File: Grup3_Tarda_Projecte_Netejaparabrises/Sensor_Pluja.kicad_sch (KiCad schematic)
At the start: 0 parts

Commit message: canvis esquematic
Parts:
- added C1: 100n, symbol Device:C
- added R1, R2: R, symbol Device:R
- added RV1: 10k, symbol Device:R_Potentiometer_Trim
- added SW1: SW_SPST, symbol Switch:SW_SPST
- added U3: LM393, symbol Comparator:LM393
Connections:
- new net: R1.2, RV1.1
- new net +VCC: C1.1, R1.1, SW1.2 (B), U3.8 (V+)
- new net Comp_o: U3.1
- new net GND: C1.2, R2.2, RV1.3, U3.4 (V-)
- new net Vin+: R2.1, SW1.1 (A), U3.3 (+)
- new net Vthold: RV1.2, U3.2 (-)
- no-connect marks 0 -> 3
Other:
- note added: "DRIVER SENSOR PLUJA"
- note added: "SENSOR"
- note added: "SENSOR PLUJA"
- note added: "SUPPLY"

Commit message: canvis esquematic
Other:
- title: (none) -> Projecte Netejaparabrises - Grup 4 Tarda
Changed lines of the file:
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@@
 (kicad_sch (version 20230121) (generator eeschema)
   (paper "A4")
+  (title_block
+    (title "Projecte Netejaparabrises - Grup 4 Tarda")
+    (date "2023-03-30")
+    (rev "v1.0.30032023")
+  )
   (junction (at 181.864 102.362) (diameter 0) (color 0 0 0 0)
   )

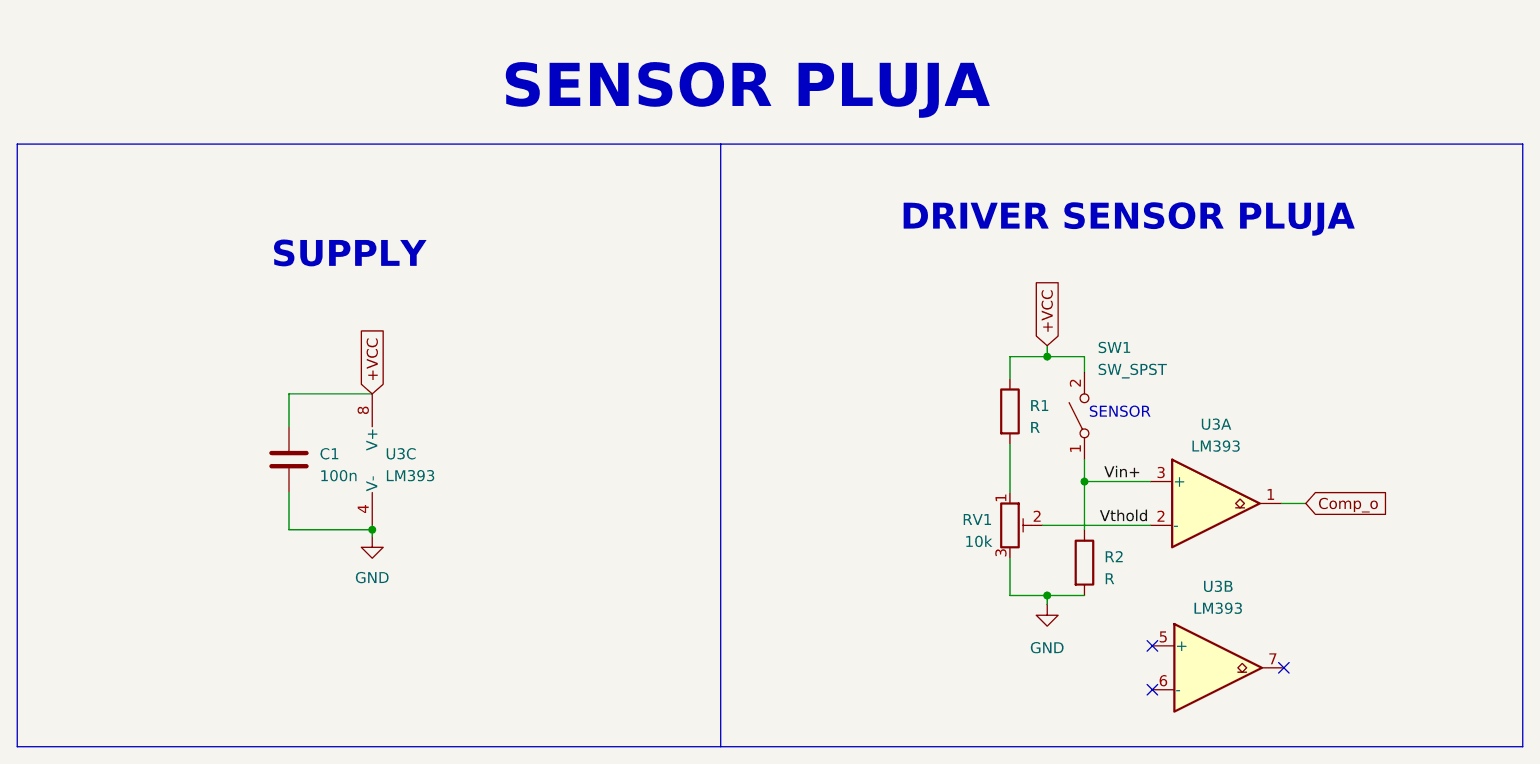
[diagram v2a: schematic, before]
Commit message: Modificat nets dels drivers de motors bombes... botonera i sensor de pluja millorats i amb connectors
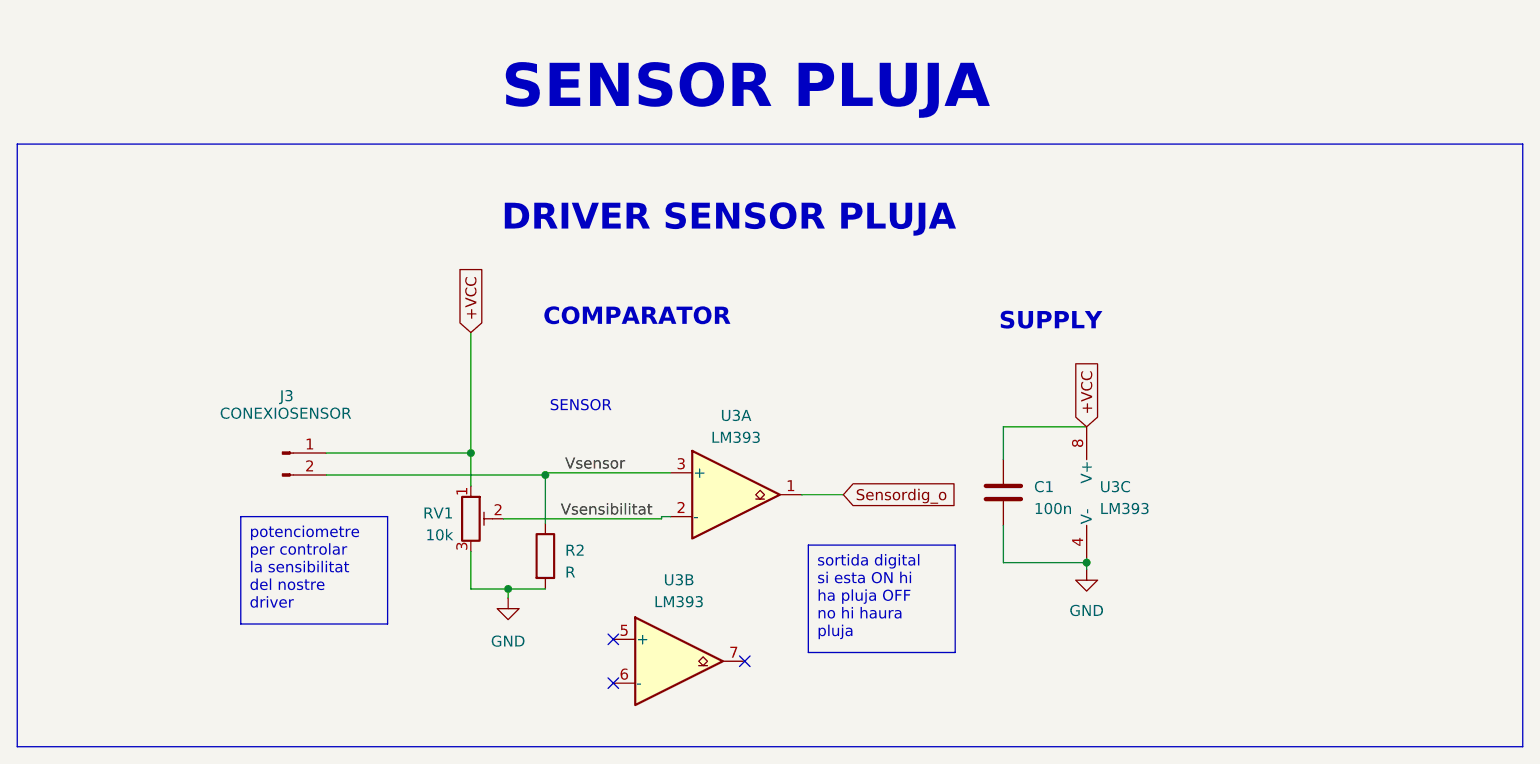
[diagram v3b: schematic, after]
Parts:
- removed R1: R, symbol Device:R
- removed SW1: SW_SPST, symbol Switch:SW_SPST
- added J3: CONEXIOSENSOR, symbol Connector:Conn_01x02_Pin
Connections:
- net +VCC: now also RV1.1, J3.1 (Pin_1)
- net Comp_o renamed Sensordig_o
- net Vin+ renamed Vsensor
- net Vsensor: now also J3.2 (Pin_2)
- net Vthold renamed Vsensibilitat
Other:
- note added: "COMPARATOR"
- moved on the sheet: C1, R2, RV1, U3A, U3B, U3C

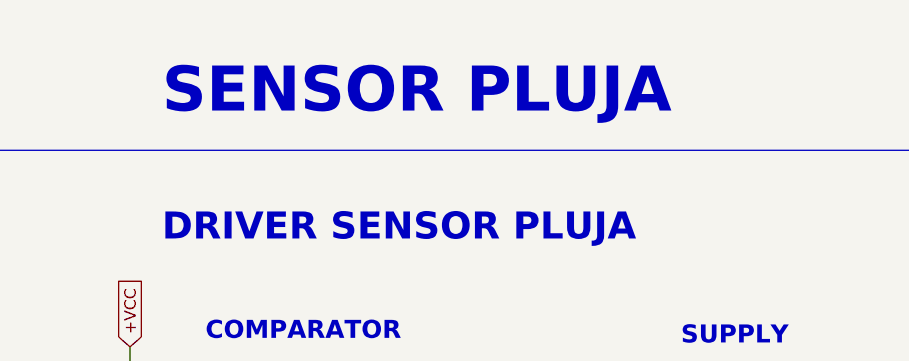
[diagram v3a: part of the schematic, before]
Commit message: Canvis estructura general, reles, comunicacacions i clock
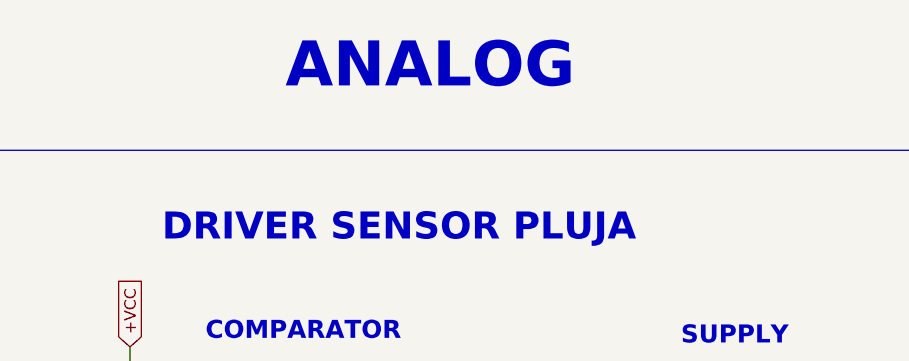
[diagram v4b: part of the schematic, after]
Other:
- note added: "ANALOG"
- note removed: "SENSOR PLUJA"
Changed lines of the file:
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@@
     (effects (font (size 3 3) bold) (justify left bottom))
   )
-  (text "SENSOR PLUJA" (at 114.3 59.69 0)
+  (text "ANALOG" (at 128.016 56.896 0)
     (effects (font (size 5 5) bold) (justify left bottom))
   )

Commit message: canvis schematic 05-04-23
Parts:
- removed unit 2 of U3
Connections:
- no-connect marks 3 -> 0
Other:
- moved on the sheet: C1, U3C

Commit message: canvis schematic i README 07-04-2023
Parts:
- U3: footprint (none) -> Package_SO:SOIC-8_3.9x4.9mm_P1.27mm
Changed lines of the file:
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@@
       (effects (font (size 1.27 1.27)))
     )
-    (property "Footprint" "" (at 141.478 103.886 0)
+    (property "Footprint" "Package_SO:SOIC-8_3.9x4.9mm_P1.27mm" (at 141.478 103.886 0)
       (effects (font (size 1.27 1.27)) hide)
     )
@@
       (effects (font (size 1.27 1.27)) (justify left))
     )
-    (property "Footprint" "" (at 188.722 103.632 0)
+    (property "Footprint" "Package_SO:SOIC-8_3.9x4.9mm_P1.27mm" (at 188.722 103.632 0)
       (effects (font (size 1.27 1.27)) hide)
     )

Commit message: GNDS 08042023
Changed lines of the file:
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@@
       (effects (font (size 1.27 1.27)) hide)
     )
-    (property "Value" "GND" (at 186.182 116.332 0)
-      (effects (font (size 1.27 1.27)))
+    (property "Value" "GND2" (at 189.23 113.411 0)
+      (effects (font (size 1.27 1.27)) (justify left))
     )
     (property "Footprint" "" (at 186.182 111.506 0)
@@
       (effects (font (size 1.27 1.27)) hide)
     )
-    (property "Value" "GND" (at 115.062 120.904 0)
-      (effects (font (size 1.27 1.27)))
+    (property "Value" "GND2" (at 118.11 117.729 0)
+      (effects (font (size 1.27 1.27)) (justify left))
     )
     (property "Footprint" "" (at 115.062 115.824 0)

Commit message: definitiuEsquematicsenseFootprints
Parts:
- RSens: renamed from R2; value R -> 1k
- renumbered C1 to CDesOpam, RV1 to RPOT
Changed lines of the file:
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@@
   (symbol (lib_id "Device:R") (at 119.38 110.998 0) (unit 1)
     (in_bom yes) (on_board yes) (dnp no) (fields_autoplaced)
-    (property "Reference" "R2" (at 121.666 110.363 0)
+    (property "Reference" "RSens" (at 121.666 110.363 0)
       (effects (font (size 1.27 1.27)) (justify left))
     )
-    (property "Value" "R" (at 121.666 112.903 0)
+    (property "Value" "1k" (at 121.666 112.903 0)
       (effects (font (size 1.27 1.27)) (justify left))
     )
@@
       (project "Grup3_Tarda_Projecte_Netejaparabrises"
         (path "/7ae78f34-680b-4fd9-8391-ce3e1c73c4b5/1911e221-32e7-4aa1-805e-6cbecb9cf221"
-          (reference "R2") (unit 1)
+          (reference "RSens") (unit 1)
         )
       )
@@
   (symbol (lib_id "Device:R_Potentiometer_Trim") (at 110.744 106.68 0) (unit 1)
     (in_bom yes) (on_board yes) (dnp no) (fields_autoplaced)
-    (property "Reference" "RV1" (at 108.712 106.045 0)
+    (property "Reference" "RPOT" (at 107.95 106.045 0)
       (effects (font (size 1.27 1.27)) (justify right))
     )
-    (property "Value" "10k" (at 108.712 108.585 0)
+    (property "Value" "10k" (at 107.95 108.585 0)
       (effects (font (size 1.27 1.27)) (justify right))
     )
@@
       (project "Grup3_Tarda_Projecte_Netejaparabrises"
         (path "/7ae78f34-680b-4fd9-8391-ce3e1c73c4b5/1911e221-32e7-4aa1-805e-6cbecb9cf221"
-          (reference "RV1") (unit 1)
+          (reference "RPOT") (unit 1)
         )
       )
@@
   (symbol (lib_id "Device:C") (at 176.53 103.632 0) (unit 1)
     (in_bom yes) (on_board yes) (dnp no)
-    (property "Reference" "C1" (at 180.086 102.997 0)
+    (property "Reference" "CDesOpam" (at 171.45 101.473 0)
       (effects (font (size 1.27 1.27)) (justify left))
     )
@@
       (project "Grup3_Tarda_Projecte_Netejaparabrises"
         (path "/7ae78f34-680b-4fd9-8391-ce3e1c73c4b5/1911e221-32e7-4aa1-805e-6cbecb9cf221"
-          (reference "C1") (unit 1)
+          (reference "CDesOpam") (unit 1)
         )
       )
@@
       (effects (font (size 1.27 1.27)) hide)
     )
-    (property "Value" "GND2" (at 189.23 113.411 0)
+    (property "Value" "GND" (at 189.23 113.411 0)
       (effects (font (size 1.27 1.27)) (justify left))
     )
@@
       (effects (font (size 1.27 1.27)) hide)
     )
-    (property "Value" "GND2" (at 118.11 117.729 0)
+    (property "Value" "GND" (at 118.11 117.729 0)
       (effects (font (size 1.27 1.27)) (justify left))
     )
